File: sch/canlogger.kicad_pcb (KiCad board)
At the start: 4 copper layers, 50 x 40 mm, 103 parts, among them J1 DE9_Pins_MountingHoles, J2 2x7P Pitch:1.27mm, Q1 NTD2955T4G, Q2 IRLML0060, Q3 IRLML0060, SW1 TS-1087S-01526, U1 STM32G474CBT6, U2 TJA1051T/3, U3 TJA1051T/3, U4 CH340N, U5 AP63205WU-7, U6 LD1117S33CTR, X1 GT-TF003-H0185-02, Y1 16MHz

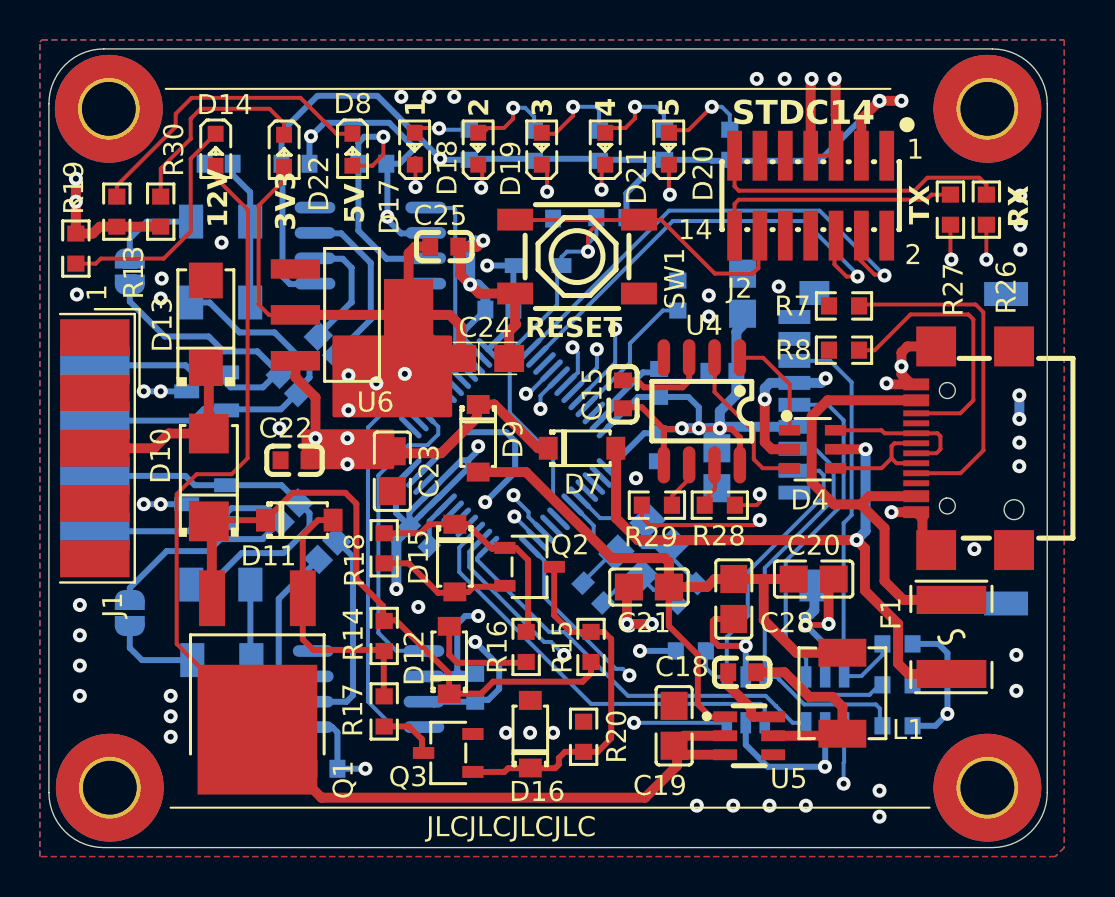
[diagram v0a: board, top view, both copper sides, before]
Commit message: v1.1 changes * increase LED resistors as they are too bright * replace solder jumpers with pins * add corresponding 3D models
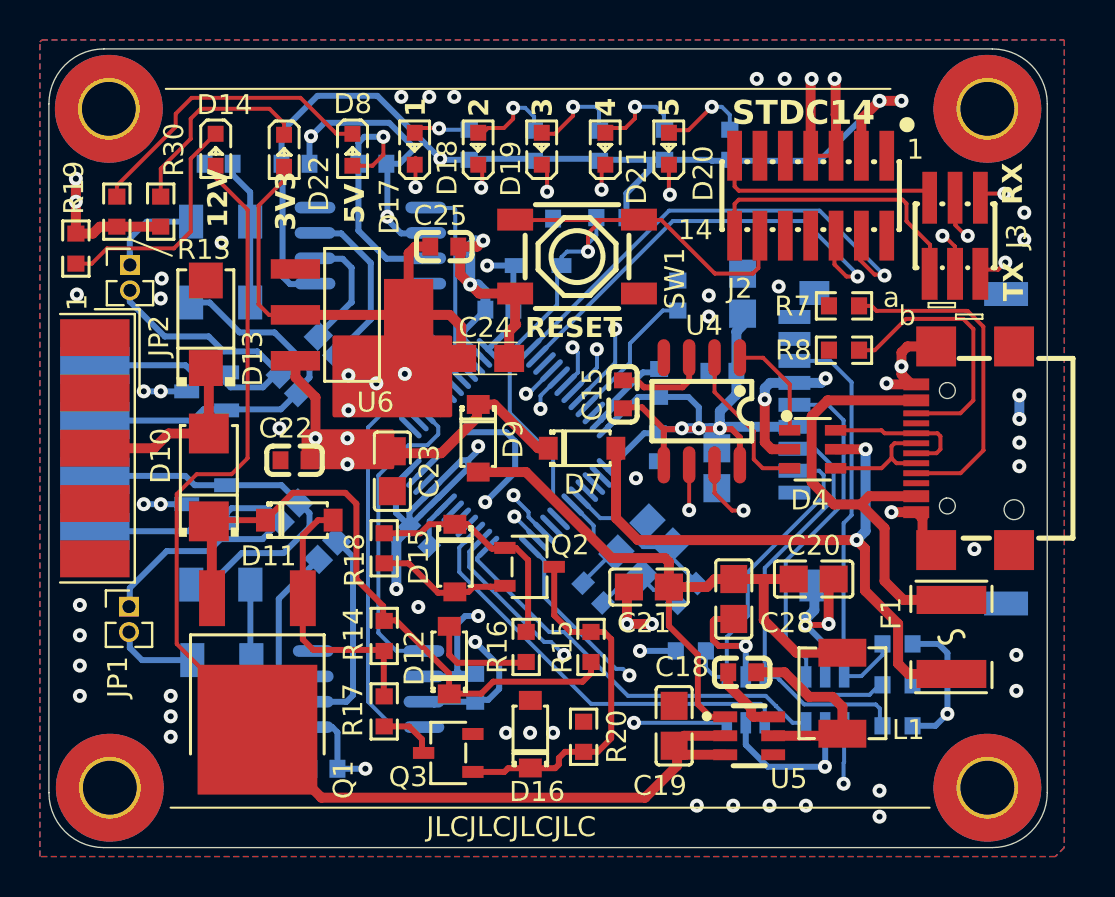
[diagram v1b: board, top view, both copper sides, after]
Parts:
- removed R26, R27, R28, R29: 0, EasyEDA_Lib:R0603
- added J3: 3x2p, 1.27, canlogger_custom_lib:HDR-SMD_6P-P1.27-V-M-R2-C3-S1.27-LS5.5-1, F.Cu at (150.4, 102.9)
- JP1, JP2: value SolderJumper_2_Open -> 2p. 1.27; footprint Jumper:SolderJumper-2_P1.3mm_Open_RoundedPad1.0x1.5mm -> canlogger_custom_lib:PinHeader_1x02_P1.27mm_Vertical; moved to F.Cu
- R13: value 1k -> 5k1
- R19: value 5k1 -> 10k
- R21, R22, R23, R24, R25, R30: value 330 -> 5k1
- moved JP2 0.33 mm to (109.1, 104.3), turned to 0 degrees
- moved JP1 0.32 mm to (109.0, 121.4), turned to 0 degrees
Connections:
- J2 pad 13: Net-(J2-Pad13) -> VCP_UART_RX
- J2 pad 14: Net-(J2-Pad14) -> VCP_UART_TX
- U1 pad 10: UART_USB_TX -> UART_TX
- U1 pad 11: UART_USB_RX -> UART_RX
- U4 pad 6: Net-(U4-TXD) -> UART_USB_RX
- U4 pad 7: Net-(U4-RXD) -> UART_USB_TX
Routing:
- net UART_RX: track 0.00 -> 33.6 mm, vias 0 -> 2
- net UART_TX: track 0.00 -> 33.2 mm, vias 0 -> 2
- net Net-(J2-Pad13): track 15.1 -> 0.00 mm
- net VCP_UART_TX: track 0.00 -> 14.4 mm
- net Net-(J2-Pad14): track 12.6 -> 0.00 mm
- net UART_USB_RX: track 40.6 -> 28.6 mm, vias 3 -> 2
- net VCP_UART_RX: track 0.00 -> 11.7 mm
- net UART_USB_TX: track 34.3 -> 25.0 mm, vias 3 -> 2
- net Net-(U4-TXD): track 2.37 -> 0.00 mm
- net Net-(U4-RXD): track 2.22 -> 0.00 mm
- net GND: vias 65 -> 64
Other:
- board text added: "a"
- board text added: "b"
- board text added: "v1.1"
- board text removed: "v1.0"
